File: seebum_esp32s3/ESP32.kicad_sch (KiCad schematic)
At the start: 55 parts, among them J201 USB_C_Receptacle_USB2.0_16P, J202 USB_C_Receptacle_USB2.0_16P, J203 Conn_02x10_Odd_Even, J204 Conn_02x10_Odd_Even, Q201 UMH3N, SW201 SW_MEC_5E, SW202 SW_MEC_5E, U201 ESP32-S3-WROOM-1, U202 CH343P, U203 AMS1117-3.3

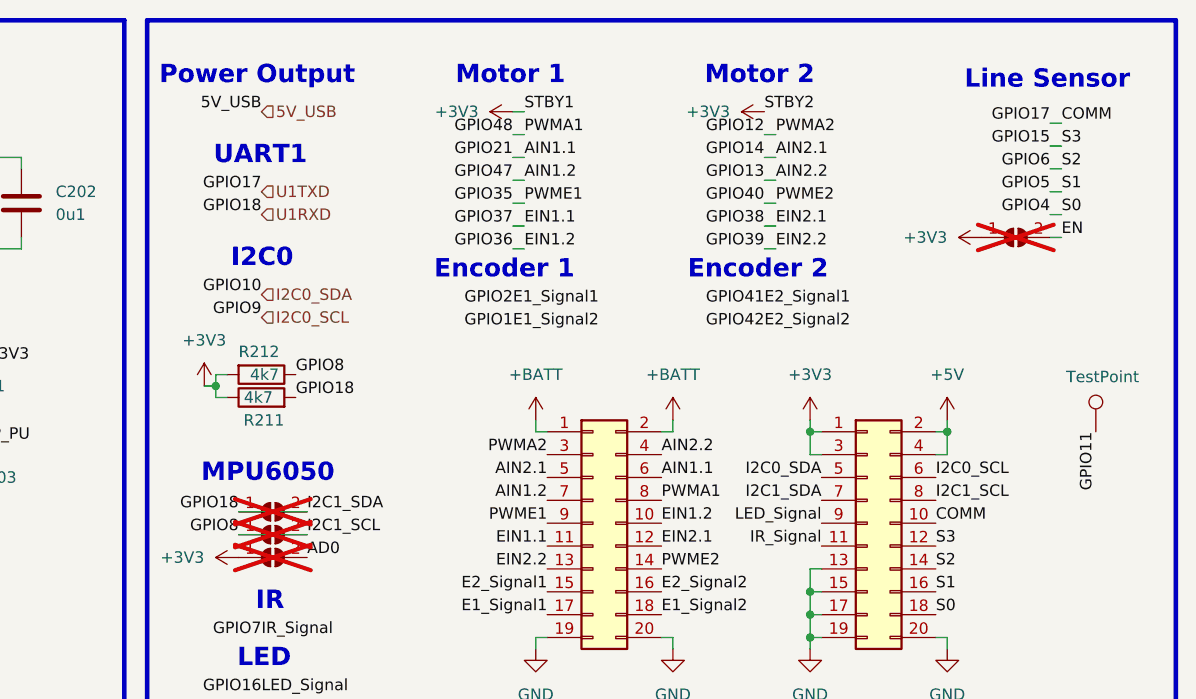
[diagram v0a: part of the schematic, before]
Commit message: Feat: fix uart1 schematic issue and I2C redundancy
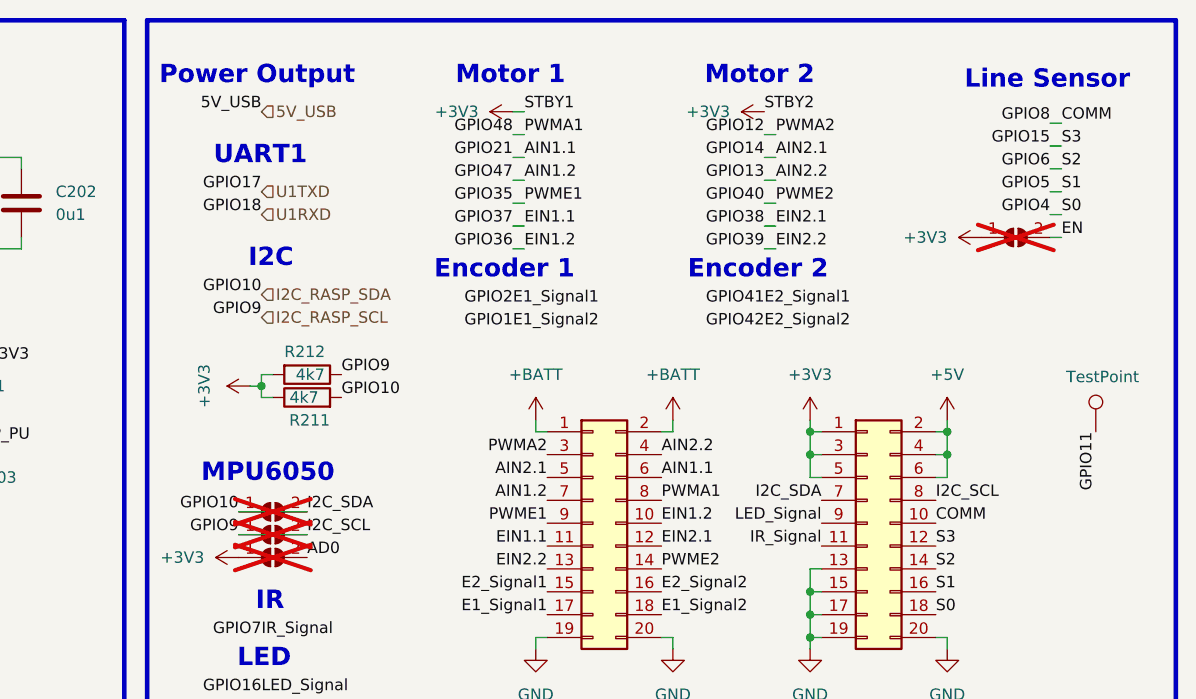
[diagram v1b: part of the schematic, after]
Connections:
- net +3V3: now also J204.5 (Pin_5)
- net +5V: now also J204.6 (Pin_6)
- net U1RXD: no longer J204.7 (Pin_7), JP204.1 (A), JP204.2 (B), R211.2
- net U1TXD: no longer J204.10 (Pin_10)
- net GPIO8 renamed I2C_RASP_SCL
- net I2C_RASP_SCL: now also U201.17 (GPIO9/TOUCH9/ADC1_CH8/FSPIHD/SUBSPIHD); no longer U201.12 (GPIO8/TOUCH8/ADC1_CH7/SUBSPICS1)
- removed net I2C0_SCL: J204.6 (Pin_6), U201.17 (GPIO9/TOUCH9/ADC1_CH8/FSPIHD/SUBSPIHD)
- net I2C0_SDA renamed I2C_RASP_SDA
- net I2C_RASP_SDA: now also J204.7 (Pin_7), JP204.1 (A), JP204.2 (B), R211.2; no longer J204.5 (Pin_5)
- new net COMM: J204.10 (Pin_10), U201.12 (GPIO8/TOUCH8/ADC1_CH7/SUBSPICS1)
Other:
- note added: "I2C"
- note removed: "I2C0"

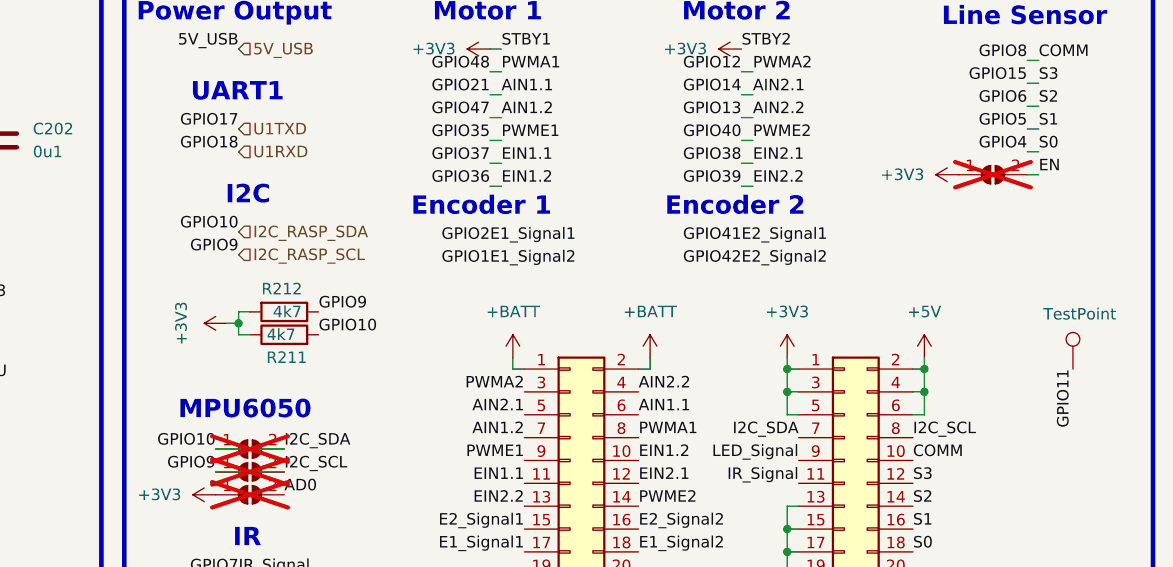
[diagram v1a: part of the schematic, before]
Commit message: Feat: I2C and UART to same pins in ESP32, since any GPIO can be RxD and TxD
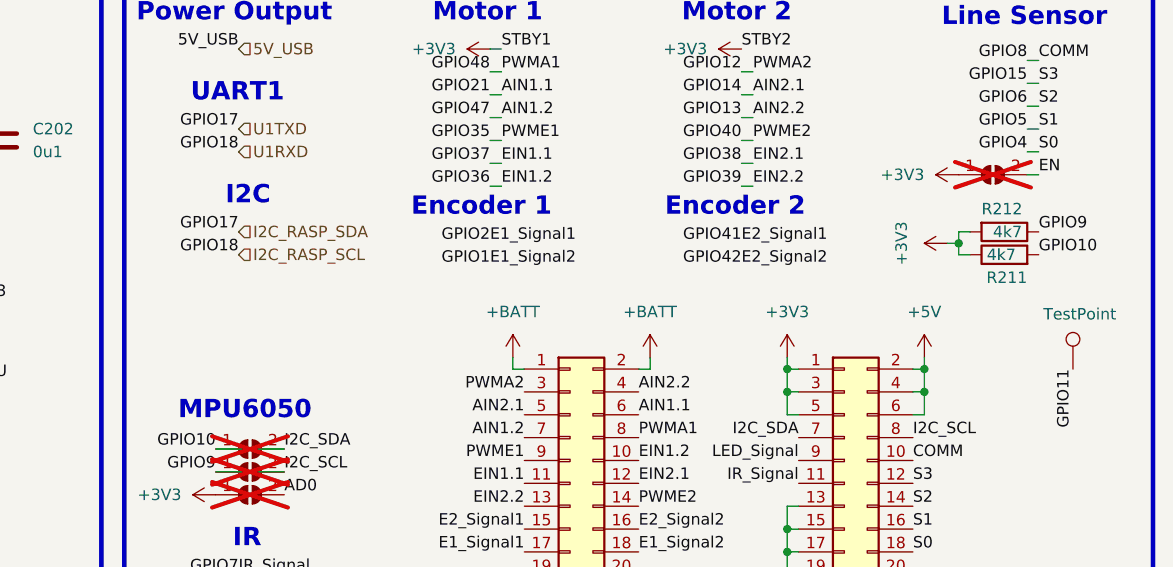
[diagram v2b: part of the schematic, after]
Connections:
- net U1RXD is gone; now on net I2C_RASP_SCL: U201.11 (GPIO18/U1RXD/ADC2_CH7/CLK_OUT3)
- net U1TXD is gone; now on net I2C_RASP_SDA: U201.10 (GPIO17/U1TXD/ADC2_CH6)
- net I2C_RASP_SCL: no longer J204.8 (Pin_8), JP205.1 (A), JP205.2 (B), R212.1, U201.17 (GPIO9/TOUCH9/ADC1_CH8/FSPIHD/SUBSPIHD)
- net I2C_RASP_SDA: no longer J204.7 (Pin_7), JP204.1 (A), JP204.2 (B), R211.2, U201.18 (GPIO10/TOUCH10/ADC1_CH9/FSPICS0/FSPIIO4/SUBSPICS0)
- new net GPIO10: J204.7 (Pin_7), JP204.1 (A), JP204.2 (B), R211.2, U201.18 (GPIO10/TOUCH10/ADC1_CH9/FSPICS0/FSPIIO4/SUBSPICS0)
- new net GPIO9: J204.8 (Pin_8), JP205.1 (A), JP205.2 (B), R212.1, U201.17 (GPIO9/TOUCH9/ADC1_CH8/FSPIHD/SUBSPIHD)
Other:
- moved on the sheet: R211, R212
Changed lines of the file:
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@@
 	)
 	(junction
-		(at 181.61 54.61)
+		(at 261.62 45.72)
 		(diameter 0)
 		(color 0 0 0 0)
@@
 	(wire
 		(pts
-			(xy 181.61 54.61) (xy 181.61 55.88)
+			(xy 261.62 45.72) (xy 261.62 46.99)
 		)
 		(stroke
@@
 	(wire
 		(pts
-			(xy 181.61 55.88) (xy 182.88 55.88)
+			(xy 261.62 46.99) (xy 262.89 46.99)
 		)
 		(stroke
@@
 	(wire
 		(pts
-			(xy 182.88 53.34) (xy 181.61 53.34)
+			(xy 262.89 44.45) (xy 261.62 44.45)
 		)
 		(stroke
@@
 	(wire
 		(pts
-			(xy 180.34 54.61) (xy 181.61 54.61)
+			(xy 260.35 45.72) (xy 261.62 45.72)
 		)
 		(stroke
@@
 	(wire
 		(pts
-			(xy 181.61 53.34) (xy 181.61 54.61)
+			(xy 261.62 44.45) (xy 261.62 45.72)
 		)
 		(stroke
@@
 		)
 	)
+	(label "GPIO18"
+		(at 181.61 46.99 180)
+		(fields_autoplaced yes)
+		(effects
+			(font
+				(size 1.27 1.27)
+			)
+			(justify right bottom)
+		)
+	)
 	(label "PWME2"
 		(at 238.76 34.29 0)
@@
 		)
 	)
-	(label "GPIO10"
-		(at 181.61 44.45 180)
-		(fields_autoplaced yes)
-		(effects
-			(font
-				(size 1.27 1.27)
-			)
-			(justify right bottom)
-		)
-	)
 	(label "GPIO38"
 		(at 115.57 88.9 0)
@@
 		)
 	)
+	(label "GPIO17"
+		(at 181.61 44.45 180)
+		(fields_autoplaced yes)
+		(effects
+			(font
+				(size 1.27 1.27)
+			)
+			(justify right bottom)
+		)
+	)
 	(label "GPIO42"
 		(at 24.13 50.8 180)
@@
 	)
 	(label "GPIO9"
-		(at 190.5 53.34 0)
+		(at 270.51 44.45 0)
 		(fields_autoplaced yes)
 		(effects
@@
 		)
 	)
-	(label "GPIO9"
-		(at 181.61 46.99 180)
-		(fields_autoplaced yes)
-		(effects
-			(font
-				(size 1.27 1.27)
-			)
-			(justify right bottom)
-		)
-	)
 	(label "GPIO1"
 		(at 209.55 48.26 180)
@@
 	)
 	(label "GPIO10"
-		(at 190.5 55.88 0)
+		(at 270.51 46.99 0)
 		(fields_autoplaced yes)
 		(effects
@@
 	(symbol
 		(lib_id "Device:R")
-		(at 186.69 55.88 90)
+		(at 266.7 46.99 90)
 		(unit 1)
 		(exclude_from_sim no)
@@
 		(dnp no)
 		(property "Reference" "R211"
-			(at 189.23 58.42 90)
+			(at 269.24 49.53 90)
 			(effects
 				(font
@@
 		)
 		(property "Value" "4k7"
-			(at 187.96 55.88 90)
+			(at 267.97 46.99 90)
 			(effects
 				(font
@@
 		)
 		(property "Footprint" "Resistor_SMD:R_0805_2012Metric"
-			(at 186.69 57.658 90)
+			(at 266.7 48.768 90)
 			(effects
 				(font
@@
 		)
 		(property "Datasheet" "~"
-			(at 186.69 55.88 0)
+			(at 266.7 46.99 0)
 			(effects
 				(font
@@
 		)
 		(property "Description" ""
-			(at 186.69 55.88 0)
+			(at 266.7 46.99 0)
 			(effects
 				(font
@@
 		)
 		(property "LCSC" "C17673"
-			(at 186.69 55.88 90)
+			(at 266.7 46.99 90)
 			(effects
 				(font
@@
 	(symbol
 		(lib_id "power:+3V3")
-		(at 180.34 54.61 90)
+		(at 260.35 45.72 90)
 		(unit 1)
 		(exclude_from_sim no)
@@
 		(fields_autoplaced yes)
 		(property "Reference" "#PWR0232"
-			(at 184.15 54.61 0)
+			(at 264.16 45.72 0)
 			(effects
 				(font
@@
 		)
 		(property "Value" "+3V3"
-			(at 175.26 54.61 0)
+			(at 255.27 45.72 0)
 			(effects
 				(font
@@
 		)
 		(property "Footprint" ""
-			(at 180.34 54.61 0)
+			(at 260.35 45.72 0)
 			(effects
 				(font
@@
 		)
 		(property "Datasheet" ""
-			(at 180.34 54.61 0)
+			(at 260.35 45.72 0)
 			(effects
 				(font
@@
 		)
 		(property "Description" ""
-			(at 180.34 54.61 0)
+			(at 260.35 45.72 0)
 			(effects
 				(font
@@
 	(symbol
 		(lib_id "Device:R")
-		(at 186.69 53.34 270)
+		(at 266.7 44.45 270)
 		(unit 1)
 		(exclude_from_sim no)
@@
 		(dnp no)
 		(property "Reference" "R212"
-			(at 184.15 50.8 90)
+			(at 264.16 41.91 90)
 			(effects
 				(font
@@
 		)
 		(property "Value" "4k7"
-			(at 185.42 53.34 90)
+			(at 265.43 44.45 90)
 			(effects
 				(font
@@
 		)
 		(property "Footprint" "Resistor_SMD:R_0805_2012Metric"
-			(at 186.69 51.562 90)
+			(at 266.7 42.672 90)
 			(effects
 				(font
@@
 		)
 		(property "Datasheet" "~"
-			(at 186.69 53.34 0)
+			(at 266.7 44.45 0)
 			(effects
 				(font
@@
 		)
 		(property "Description" ""
-			(at 186.69 53.34 0)
+			(at 266.7 44.45 0)
 			(effects
 				(font
@@
 		)
 		(property "LCSC" "C17673"
-			(at 186.69 53.34 90)
+			(at 266.7 44.45 90)
 			(effects
 				(font

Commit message: Feat: final revision
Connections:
- net +3V3: now also C211.2, C212.2, U202.1 (VIO), U202.3 (VDD5)
- net GPIO0: now also U201.27 (GPIO0/BOOT)
- net U0RXD: now also JP203.1 (A); no longer JP202.1 (A)
- net U0TXD: now also JP202.1 (A); no longer JP203.1 (A)
- no-connect marks 13 -> 12
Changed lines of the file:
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@@
 	)
 	(junction
+		(at 130.81 134.62)
+		(diameter 0)
+		(color 0 0 0 0)
+	)
+	(junction
 		(at 257.81 62.23)
 		(diameter 0)
@@
 	)
 	(junction
+		(at 130.81 139.7)
+		(diameter 0)
+		(color 0 0 0 0)
+	)
+	(junction
 		(at 148.59 26.67)
 		(diameter 0)
@@
 	)
 	(no_connect
-		(at 115.57 43.18)
-	)
-	(no_connect
 		(at 209.55 146.05)
 	)
@@
 	(wire
 		(pts
+			(xy 130.81 129.54) (xy 130.81 134.62)
+		)
+		(stroke
+			(width 0)
+			(type default)
+		)
+	)
+	(wire
+		(pts
 			(xy 264.16 114.3) (xy 264.16 139.7)
 		)
@@
 	(wire
 		(pts
-			(xy 127 134.62) (xy 132.08 134.62)
+			(xy 127 134.62) (xy 130.81 134.62)
 		)
 		(stroke
@@
 	(wire
 		(pts
+			(xy 130.81 134.62) (xy 130.81 139.7)
+		)
+		(stroke
+			(width 0)
+			(type default)
+		)
+	)
+	(wire
+		(pts
 			(xy 260.35 132.08) (xy 260.35 134.62)
 		)
@@
 	(wire
 		(pts
+			(xy 130.81 139.7) (xy 132.08 139.7)
+		)
+		(stroke
+			(width 0)
+			(type default)
+		)
+	)
+	(wire
+		(pts
 			(xy 142.24 29.21) (xy 148.59 29.21)
 		)
@@
 	(wire
 		(pts
-			(xy 127 139.7) (xy 132.08 139.7)
+			(xy 127 139.7) (xy 130.81 139.7)
 		)
 		(stroke
@@
 	(wire
 		(pts
+			(xy 130.81 134.62) (xy 132.08 134.62)
+		)
+		(stroke
+			(width 0)
+			(type default)
+		)
+	)
+	(wire
+		(pts
 			(xy 271.78 148.59) (xy 267.97 148.59)
 		)
@@
 		)
 	)
-	(label "U0RXD"
+	(label "U0TXD"
 		(at 113.03 153.67 0)
 		(fields_autoplaced yes)
@@
 		)
 	)
+	(label "GPIO0"
+		(at 115.57 43.18 0)
+		(fields_autoplaced yes)
+		(effects
+			(font
+				(size 1.27 1.27)
+			)
+			(justify left bottom)
+		)
+	)
 	(label "GPIO38"
 		(at 115.57 88.9 0)
@@
 		)
 	)
-	(label "U0TXD"
+	(label "U0RXD"
 		(at 113.03 147.32 0)
 		(fields_autoplaced yes)
@@
 					(unit 1)
 				)
+			)
+		)
+	)
+	(symbol
+		(lib_id "power:+3V3")
+		(at 130.81 129.54 0)
+		(unit 1)
+		(exclude_from_sim no)
+		(in_bom yes)
+		(on_board yes)
+		(dnp no)
+		(fields_autoplaced yes)
+		(property "Reference" "#PWR0236"
+			(at 130.81 133.35 0)
+			(effects
+				(font
+					(size 1.27 1.27)
+				)
+				(hide yes)
+			)
+		)
+		(property "Value" "+3V3"
+			(at 130.81 124.46 0)
+			(effects
+				(font
+					(size 1.27 1.27)
+				)
+			)
+		)
+		(property "Footprint" ""
+			(at 130.81 129.54 0)
+			(effects
+				(font
+					(size 1.27 1.27)
+				)
+				(hide yes)
+			)
+		)
+		(property "Datasheet" ""
+			(at 130.81 129.54 0)
+			(effects
+				(font
+					(size 1.27 1.27)
+				)
+				(hide yes)
+			)
+		)
+		(property "Description" "Power symbol creates a global label with name \"+3V3\""
+			(at 130.81 129.54 0)
+			(effects
+				(font
+					(size 1.27 1.27)
+				)
+				(hide yes)
+			)
+		)
+		(pin "1"
+		)
+		(instances
+			(project "seebum_esp32s3"
+				(path "/4eaa6483-1d2f-48d6-89f0-93b42e27355e/995310a1-b122-49d8-8098-d1cf0e8f38bd"
+					(reference "#PWR0236")
+					(unit 1)
+				)
